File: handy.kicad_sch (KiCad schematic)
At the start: 5 parts, among them U1 TCA9548ARGER, U2 AS5600L-ASOM

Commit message: encoders and outline
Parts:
- added C2: 100nF, Capacitor_SMD:C_0603_1608Metric, symbol Device:C
- added J1, J2: JST-SH 1x4, Connector_JST:JST_SH_BM04B-SRSS-TB_1x04-1MP_P1.00mm_Vertical, symbol Connector_Generic_MountingPin:Conn_01x04_MountingPin
- added JP1, JP2, JP3: ~, Resistor_SMD:R_0201_0603Metric, symbol Jumper:SolderJumper_2_Open
- added R3, R4: 4.7k, Resistor_SMD:R_0201_0603Metric, symbol Device:R
- added R7, R8, R9: 100k, Resistor_SMD:R_0201_0603Metric, symbol Device:R
- added U3: AS5600L-ASOM, footprints:AS5600L-ASOM_AMS, symbol as5600:AS5600L-ASOM
- C1: footprint Capacitor_SMD:C_0805_2012Metric -> Capacitor_SMD:C_0603_1608Metric
- R1, R2: footprint Resistor_SMD:R_0805_2012Metric -> Resistor_SMD:R_0201_0603Metric
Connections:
- net 3.3V is gone; now on net +3.3V: C1.1, R1.1, R2.1, U2.1 (VDD5V), U2.2 (VDD3V3)
- net GND: now also U1.9 (GND), U2.8 (DIR), C2.2, J1.4 (Pin_4), J2.4 (Pin_4), R7.2, R8.2, R9.2, U3.4 (GND), U3.8 (DIR)
- net SCL0: now also U1.11 (SC4); no longer U1.2 (SC0)
- net SCL1: now also U1.8 (SC3), R3.2, U3.7 (SCL); no longer U1.4 (SC1)
- net SDA0: now also U1.10 (SD4); no longer U1.1 (SD0)
- net SDA1: now also U1.7 (SD3), R4.2, U3.6 (SDA); no longer U1.3 (SD1)
- net ADDR_2: now reaches U1.18 (A2)
- net ADDR_2: now also JP3.2 (B), R9.1
- net SCL: now reaches U1.19 (SCL)
- net SCL: now also J1.1 (Pin_1), J2.1 (Pin_1)
- net SDA: now reaches U1.20 (SDA)
- net SDA: now also J1.2 (Pin_2), J2.2 (Pin_2)
- net +3.3V: now reaches U1.21 (VCC)
- net +3.3V: now also C2.1, J1.3 (Pin_3), J2.3 (Pin_3), JP1.2 (B), JP2.1 (A), JP3.1 (A), R3.1, R4.1, U3.1 (VDD5V), U3.2 (VDD3V3)
- net ADDR_0: now reaches U1.22 (A0)
- net ADDR_0: now also JP1.1 (A), R7.1
- net ADDR_1: now reaches U1.23 (A1)
- net ADDR_1: now also JP2.2 (B), R8.1
- no-connect marks 3 -> 4
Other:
- moved on the sheet: C1

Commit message: first draft
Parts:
- added H1: MountingHole, MountingHole:MountingHole_2.2mm_M2_ISO14580_Pad, symbol Mechanical:MountingHole
- added M1: Motor 1, Connector_PinHeader_2.00mm:PinHeader_1x02_P2.00mm_Vertical, symbol Connector:Conn_01x02_Pin
- added M2: Motor 2, Connector_PinHeader_2.00mm:PinHeader_1x02_P2.00mm_Vertical, symbol Connector:Conn_01x02_Pin
- added U4: DRV8830DGQR, DRV8830:DGQ10_2P18X1P72, symbol drv8830:DRV8830DGQR
- added U5: ICM-42670-P, ICM42670:LGA14_2.5X3X0.76_IVS, symbol icm42670:ICM-42670-P
- C1, C2: footprint Capacitor_SMD:C_0603_1608Metric -> Capacitor_SMD:C_0201_0603Metric
- JP1, JP2, JP3: footprint Resistor_SMD:R_0201_0603Metric -> Resistor_SMD:R_0201_0603Metric_Pad0.64x0.40mm_HandSolder
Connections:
- net +3.3V: now also U4.4 (VCC), U5.12 (AP_CS), U5.5 (VDDIO), U5.8 (VDD)
- net GND: now also M1.1 (Pin_1), M2.1 (Pin_1), U4.2 (ISENSE), U4.5 (GND), U4.7 (A0), U4.8 (A1), U4.EPAD, U5.1 (AP_SDO/AP_AD0), U5.6 (GND)
- net SCL0: now also U1.2 (SC0), U4.10 (SCL), U5.13 (AP_SCL/AP_SCLK); no longer U1.11 (SC4)
- net SCL1: now also U1.11 (SC4); no longer U1.8 (SC3)
- net SDA0: now also U1.1 (SD0), U4.9 (SDA), U5.14 (AP_SDA/AP_SDIO/AP_SDI); no longer U1.10 (SD4)
- net SDA1: now also U1.10 (SD4); no longer U1.7 (SD3)
- new net M1: M1.2 (Pin_2), U4.3 (OUT1)
- new net M2: M2.2 (Pin_2), U4.1 (OUT2)
- no-connect marks 4 -> 8

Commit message: fuck my chungus life
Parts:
- C1, C2: footprint Capacitor_SMD:C_0201_0603Metric -> Capacitor_SMD:C_0603_1608Metric
- JP1, JP2, JP3: footprint Resistor_SMD:R_0201_0603Metric_Pad0.64x0.40mm_HandSolder -> Jumper:SolderJumper-2_P1.3mm_Open_TrianglePad1.0x1.5mm
- R1, R2, R3, R4, R7, R8, R9: footprint Resistor_SMD:R_0201_0603Metric -> Resistor_SMD:R_0603_1608Metric
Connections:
- no-connect marks 8 -> 9
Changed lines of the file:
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@@
 	)
 	(no_connect
+		(at 213.36 161.29)
+	)
+	(no_connect
 		(at 134.62 137.16)
 	)
@@
 			)
 		)
-		(property "Footprint" "Resistor_SMD:R_0201_0603Metric_Pad0.64x0.40mm_HandSolder"
+		(property "Footprint" "Jumper:SolderJumper-2_P1.3mm_Open_TrianglePad1.0x1.5mm"
 			(at 30.48 74.93 0)
 			(effects
@@
 		(exclude_from_sim no)
 		(in_bom yes)
-		(on_board yes)
+		(on_board no)
 		(dnp no)
 		(property "Reference" "#PWR020"
@@
 		(exclude_from_sim no)
 		(in_bom yes)
-		(on_board yes)
+		(on_board no)
 		(dnp no)
 		(property "Reference" "#PWR021"
@@
 			)
 		)
-		(property "Footprint" "Resistor_SMD:R_0201_0603Metric_Pad0.64x0.40mm_HandSolder"
+		(property "Footprint" "Jumper:SolderJumper-2_P1.3mm_Open_TrianglePad1.0x1.5mm"
 			(at 30.48 64.77 0)
 			(effects
@@
 			)
 		)
-		(property "Footprint" "Resistor_SMD:R_0201_0603Metric"
+		(property "Footprint" "Resistor_SMD:R_0603_1608Metric"
 			(at 47.752 90.17 90)
 			(effects
@@
 			)
 		)
-		(property "Footprint" "Capacitor_SMD:C_0201_0603Metric"
+		(property "Footprint" "Capacitor_SMD:C_0603_1608Metric"
 			(at 103.8352 62.23 0)
 			(effects
@@
 		(exclude_from_sim no)
 		(in_bom yes)
-		(on_board yes)
+		(on_board no)
 		(dnp no)
 		(fields_autoplaced yes)
@@
 			)
 		)
-		(property "Footprint" "Resistor_SMD:R_0201_0603Metric"
+		(property "Footprint" "Resistor_SMD:R_0603_1608Metric"
 			(at 52.832 85.09 90)
 			(effects
@@
 		(exclude_from_sim no)
 		(in_bom yes)
-		(on_board yes)
+		(on_board no)
 		(dnp no)
 		(fields_autoplaced yes)
@@
 			)
 		)
-		(property "Footprint" "Resistor_SMD:R_0201_0603Metric"
+		(property "Footprint" "Resistor_SMD:R_0603_1608Metric"
 			(at 174.752 36.83 90)
 			(effects
@@
 		(exclude_from_sim no)
 		(in_bom yes)
-		(on_board yes)
+		(on_board no)
 		(dnp no)
 		(fields_autoplaced yes)
@@
 			)
 		)
-		(property "Footprint" "Resistor_SMD:R_0201_0603Metric_Pad0.64x0.40mm_HandSolder"
+		(property "Footprint" "Jumper:SolderJumper-2_P1.3mm_Open_TrianglePad1.0x1.5mm"
 			(at 30.48 69.85 0)
 			(effects
@@
 			)
 		)
-		(property "Footprint" "Resistor_SMD:R_0201_0603Metric"
+		(property "Footprint" "Resistor_SMD:R_0603_1608Metric"
 			(at 165.862 36.83 90)
 			(effects
@@
 			)
 		)
-		(property "Footprint" "Capacitor_SMD:C_0201_0603Metric"
+		(property "Footprint" "Capacitor_SMD:C_0603_1608Metric"
 			(at 103.8352 101.6 0)
 			(effects
@@
 			)
 		)
-		(property "Footprint" "Resistor_SMD:R_0201_0603Metric"
+		(property "Footprint" "Resistor_SMD:R_0603_1608Metric"
 			(at 174.752 76.2 90)
 			(effects
@@
 			)
 		)
-		(property "Footprint" "Resistor_SMD:R_0201_0603Metric"
+		(property "Footprint" "Resistor_SMD:R_0603_1608Metric"
 			(at 42.672 96.52 90)
 			(effects
@@
 			)
 		)
-		(property "Footprint" "Resistor_SMD:R_0201_0603Metric"
+		(property "Footprint" "Resistor_SMD:R_0603_1608Metric"
 			(at 165.862 76.2 90)
 			(effects

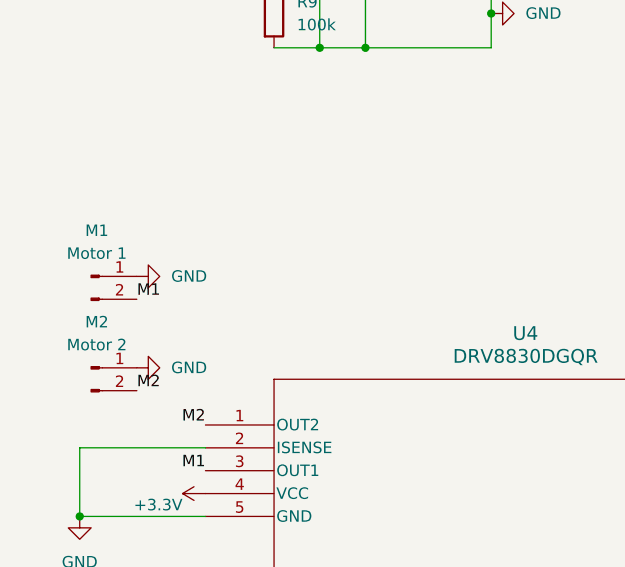
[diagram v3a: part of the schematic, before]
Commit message: routed without imu
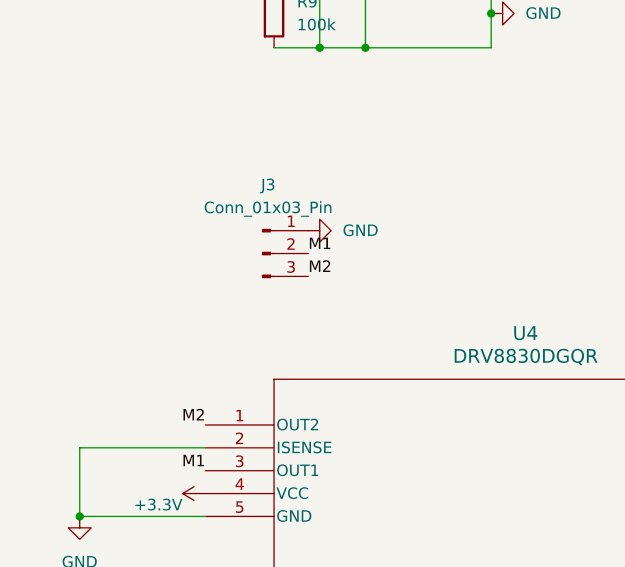
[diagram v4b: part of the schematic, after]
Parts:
- removed M1: Motor 1, Connector_PinHeader_2.00mm:PinHeader_1x02_P2.00mm_Vertical, symbol Connector:Conn_01x02_Pin
- removed M2: Motor 2, Connector_PinHeader_2.00mm:PinHeader_1x02_P2.00mm_Vertical, symbol Connector:Conn_01x02_Pin
- added J3: Conn_01x03_Pin, Connector_PinSocket_2.00mm:PinSocket_1x03_P2.00mm_Vertical, symbol Connector:Conn_01x03_Pin
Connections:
- net GND: now also J3.1 (Pin_1)
- net M1: now also J3.2 (Pin_2)
- net M2: now also J3.3 (Pin_3)
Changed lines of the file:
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@@
 	)
 	(label "M2"
-		(at 29.21 138.43 0)
+		(at 48.26 125.73 0)
 		(effects
 			(font
@@
 	)
 	(label "M1"
-		(at 29.21 128.27 0)
+		(at 48.26 123.19 0)
 		(effects
 			(font
@@
 	)
 	(symbol
-		(lib_id "power:GND")
-		(at 29.21 135.89 90)
-		(unit 1)
-		(exclude_from_sim no)
-		(in_bom yes)
-		(on_board yes)
-		(dnp no)
-		(fields_autoplaced yes)
-		(property "Reference" "#PWR019"
-			(at 35.56 135.89 0)
-			(effects
-				(font
-					(size 1.27 1.27)
-				)
-				(hide yes)
-			)
-		)
-		(property "Value" "GND"
-			(at 33.02 135.8899 90)
-			(effects
-				(font
-					(size 1.27 1.27)
-				)
-				(justify right)
-			)
-		)
-		(property "Footprint" ""
-			(at 29.21 135.89 0)
-			(effects
-				(font
-					(size 1.27 1.27)
-				)
-				(hide yes)
-			)
-		)
-		(property "Datasheet" ""
-			(at 29.21 135.89 0)
-			(effects
-				(font
-					(size 1.27 1.27)
-				)
-				(hide yes)
-			)
-		)
-		(property "Description" "Power symbol creates a global label with name \"GND\" , ground"
-			(at 29.21 135.89 0)
-			(effects
-				(font
-					(size 1.27 1.27)
-				)
-				(hide yes)
-			)
-		)
-		(pin "1"
-		)
-		(instances
-			(project "handy"
-				(path "/3e14f85b-1fd4-4034-9146-b5c17fdb3f6d"
-					(reference "#PWR019")
-					(unit 1)
-				)
-			)
-		)
-	)
-	(symbol
 		(lib_id "power:+3.3V")
 		(at 124.46 139.7 90)
@@
 	)
 	(symbol
+		(lib_id "Connector:Conn_01x03_Pin")
+		(at 43.18 123.19 0)
+		(unit 1)
+		(exclude_from_sim no)
+		(in_bom yes)
+		(on_board yes)
+		(dnp no)
+		(fields_autoplaced yes)
+		(property "Reference" "J3"
+			(at 43.815 115.57 0)
+			(effects
+				(font
+					(size 1.27 1.27)
+				)
+			)
+		)
+		(property "Value" "Conn_01x03_Pin"
+			(at 43.815 118.11 0)
+			(effects
+				(font
+					(size 1.27 1.27)
+				)
+			)
+		)
+		(property "Footprint" "Connector_PinSocket_2.00mm:PinSocket_1x03_P2.00mm_Vertical"
+			(at 43.18 123.19 0)
+			(effects
+				(font
+					(size 1.27 1.27)
+				)
+				(hide yes)
+			)
+		)
+		(property "Datasheet" "~"
+			(at 43.18 123.19 0)
+			(effects
+				(font
+					(size 1.27 1.27)
+				)
+				(hide yes)
+			)
+		)
+		(property "Description" "Generic connector, single row, 01x03, script generated"
+			(at 43.18 123.19 0)
+			(effects
+				(font
+					(size 1.27 1.27)
+				)
+				(hide yes)
+			)
+		)
+		(pin "2"
+		)
+		(pin "3"
+		)
+		(pin "1"
+		)
+		(instances
+			(project ""
+				(path "/3e14f85b-1fd4-4034-9146-b5c17fdb3f6d"
+					(reference "J3")
+					(unit 1)
+				)
+			)
+		)
+	)
+	(symbol
 		(lib_id "icm42670:ICM-42670-P")
 		(at 134.62 129.54 0)
@@
 	(symbol
 		(lib_id "power:GND")
-		(at 29.21 125.73 90)
+		(at 48.26 120.65 90)
 		(unit 1)
 		(exclude_from_sim no)
@@
 		(fields_autoplaced yes)
 		(property "Reference" "#PWR018"
-			(at 35.56 125.73 0)
+			(at 54.61 120.65 0)
 			(effects
 				(font
@@
 		)
 		(property "Value" "GND"
-			(at 33.02 125.7299 90)
+			(at 52.07 120.6499 90)
 			(effects
 				(font
@@
 		)
 		(property "Footprint" ""
-			(at 29.21 125.73 0)
+			(at 48.26 120.65 0)
 			(effects
 				(font
@@
 		)
 		(property "Datasheet" ""
-			(at 29.21 125.73 0)
+			(at 48.26 120.65 0)
 			(effects
 				(font
@@
 		)
 		(property "Description" "Power symbol creates a global label with name \"GND\" , ground"
-			(at 29.21 125.73 0)
+			(at 48.26 120.65 0)
 			(effects
 				(font
@@
 	)
 	(symbol
-		(lib_id "Connector:Conn_01x02_Pin")
-		(at 24.13 135.89 0)
-		(unit 1)
-		(exclude_from_sim no)
-		(in_bom yes)
-		(on_board yes)
-		(dnp no)
-		(fields_autoplaced yes)
-		(property "Reference" "M2"
-			(at 24.765 130.81 0)
-			(effects
-				(font
-					(size 1.27 1.27)
-				)
-			)
-		)
-		(property "Value" "Motor 2"
-			(at 24.765 133.35 0)
-			(effects
-				(font
-					(size 1.27 1.27)
-				)
-			)
-		)
-		(property "Footprint" "Connector_PinHeader_2.00mm:PinHeader_1x02_P2.00mm_Vertical"
-			(at 24.13 135.89 0)
-			(effects
-				(font
-					(size 1.27 1.27)
-				)
-				(hide yes)
-			)
-		)
-		(property "Datasheet" "~"
-			(at 24.13 135.89 0)
-			(effects
-				(font
-					(size 1.27 1.27)
-				)
-				(hide yes)
-			)
-		)
-		(property "Description" "Generic connector, single row, 01x02, script generated"
-			(at 24.13 135.89 0)
-			(effects
-				(font
-					(size 1.27 1.27)
-				)
-				(hide yes)
-			)
-		)
-		(pin "2"
-		)
-		(pin "1"
-		)
-		(instances
-			(project "handy"
-				(path "/3e14f85b-1fd4-4034-9146-b5c17fdb3f6d"
-					(reference "M2")
-					(unit 1)
-				)
-			)
-		)
-	)
-	(symbol
 		(lib_id "Device:R")
 		(at 167.64 76.2 0)
@@
 					(unit 1)
 				)
-			)
-		)
-	)
-	(symbol
-		(lib_id "Connector:Conn_01x02_Pin")
-		(at 24.13 125.73 0)
-		(unit 1)
-		(exclude_from_sim no)
-		(in_bom yes)
-		(on_board yes)
-		(dnp no)
-		(fields_autoplaced yes)
-		(property "Reference" "M1"
-			(at 24.765 120.65 0)
-			(effects
-				(font
-					(size 1.27 1.27)
-				)
-			)
-		)
-		(property "Value" "Motor 1"
-			(at 24.765 123.19 0)
-			(effects
-				(font
-					(size 1.27 1.27)
-				)
-			)
-		)
-		(property "Footprint" "Connector_PinHeader_2.00mm:PinHeader_1x02_P2.00mm_Vertical"
-			(at 24.13 125.73 0)
-			(effects
-				(font
-					(size 1.27 1.27)
-				)
-				(hide yes)
-			)
-		)
-		(property "Datasheet" "~"
-			(at 24.13 125.73 0)
-			(effects
-				(font
-					(size 1.27 1.27)
-				)
-				(hide yes)
-			)
-		)
-		(property "Description" "Generic connector, single row, 01x02, script generated"
-			(at 24.13 125.73 0)
-			(effects
-				(font
-					(size 1.27 1.27)
-				)
-				(hide yes)
-			)
-		)
-		(pin "2"
-		)
-		(pin "1"
-		)
-		(instances
-			(project ""
-				(path "/3e14f85b-1fd4-4034-9146-b5c17fdb3f6d"
-					(reference "M1")
-					(unit 1)
-				)

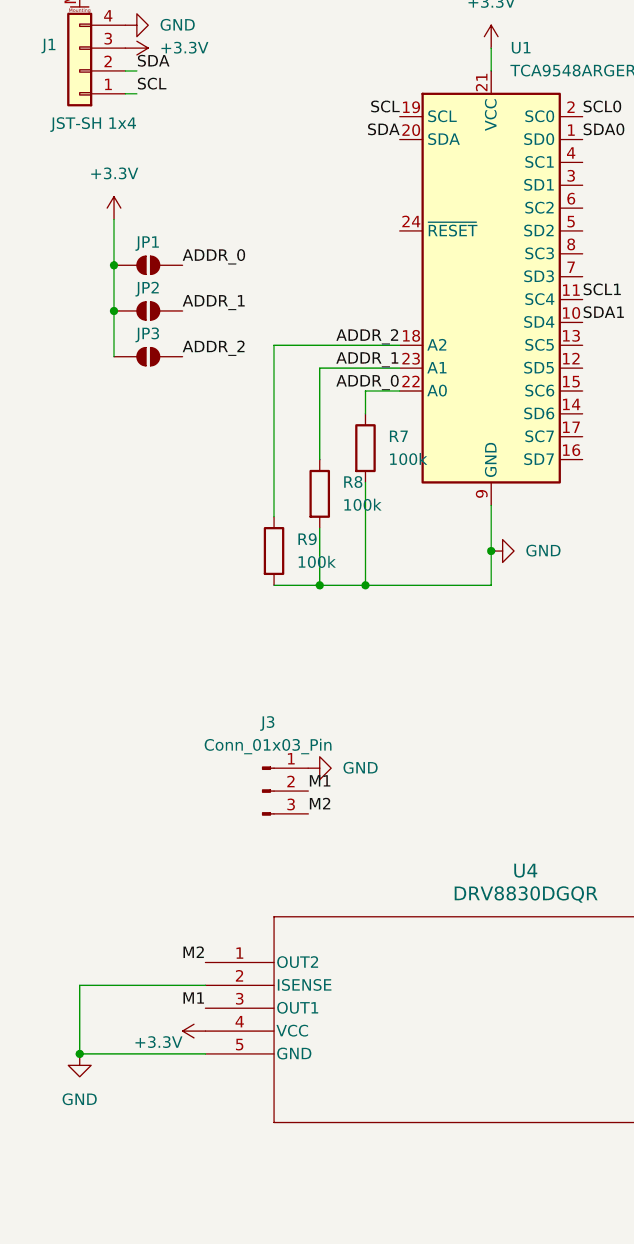
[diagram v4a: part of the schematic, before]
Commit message: added missing pullup and capacitor
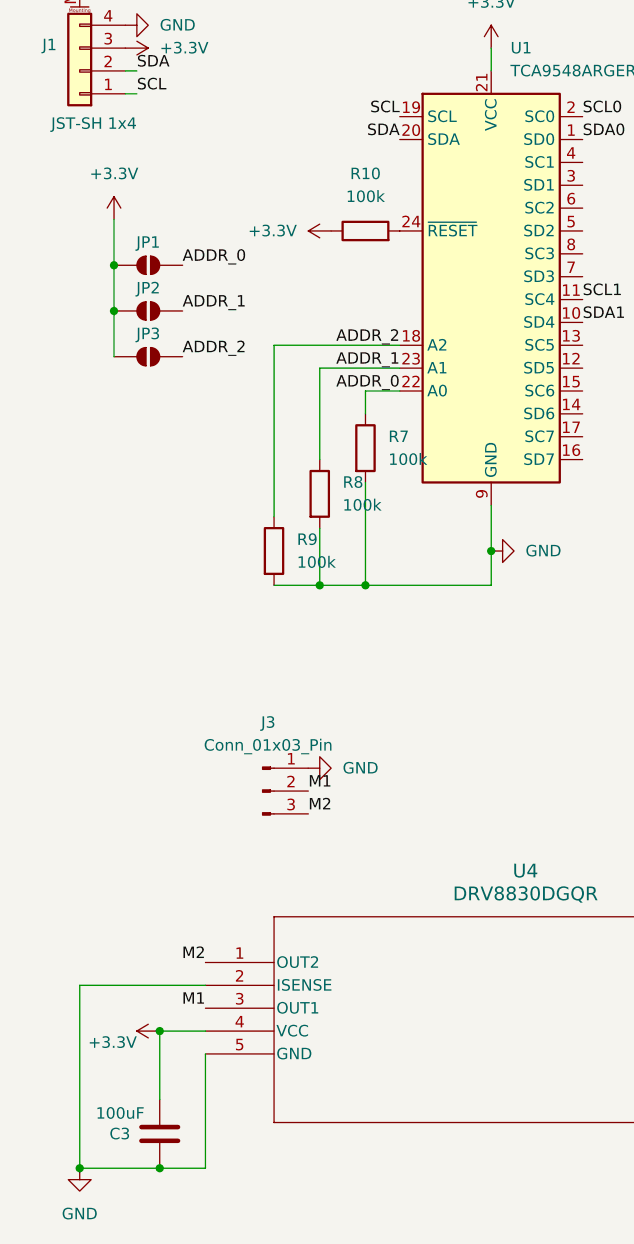
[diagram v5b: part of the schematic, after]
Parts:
- added C3: 100uF, Capacitor_SMD:C_0603_1608Metric, symbol Device:C
- added R10: 100k, Resistor_SMD:R_0603_1608Metric, symbol Device:R
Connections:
- net +3.3V: now also C3.2, R10.1
- net GND: now also C3.1
- net at U1.24 (~{RESET}): now also R10.2

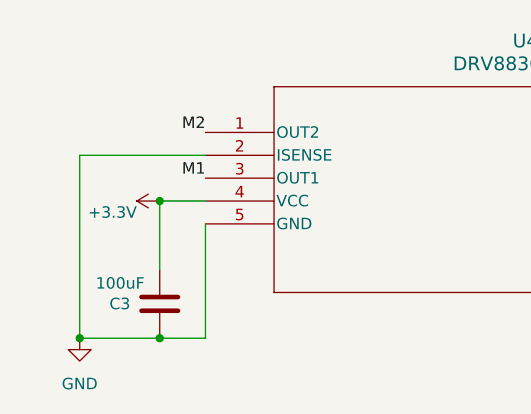
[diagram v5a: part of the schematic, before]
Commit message: fixed resistor values
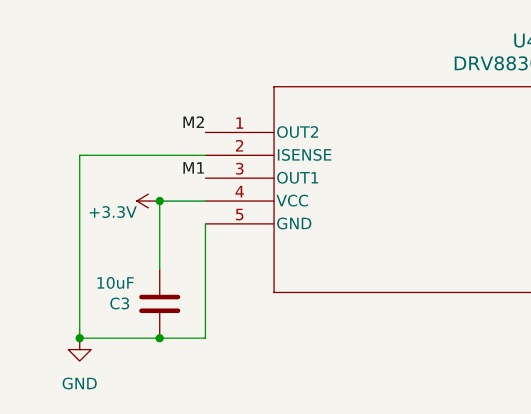
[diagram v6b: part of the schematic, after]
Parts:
- C3: value 100uF -> 10uF
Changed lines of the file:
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@@
 			)
 		)
-		(property "Value" "100uF"
+		(property "Value" "10uF"
 			(at 24.638 159.004 0)
 			(effects
